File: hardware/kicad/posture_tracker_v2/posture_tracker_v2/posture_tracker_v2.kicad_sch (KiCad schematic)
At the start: 18 parts, among them J1 GCT_USB4135-GF-A, J2 JST-PH-2, U1 ESP32-S3-MINI-1U, U2 MPU-6050, U5 MCP73831T-2ACI/OT, U6 AP2112K-3.3TRG1

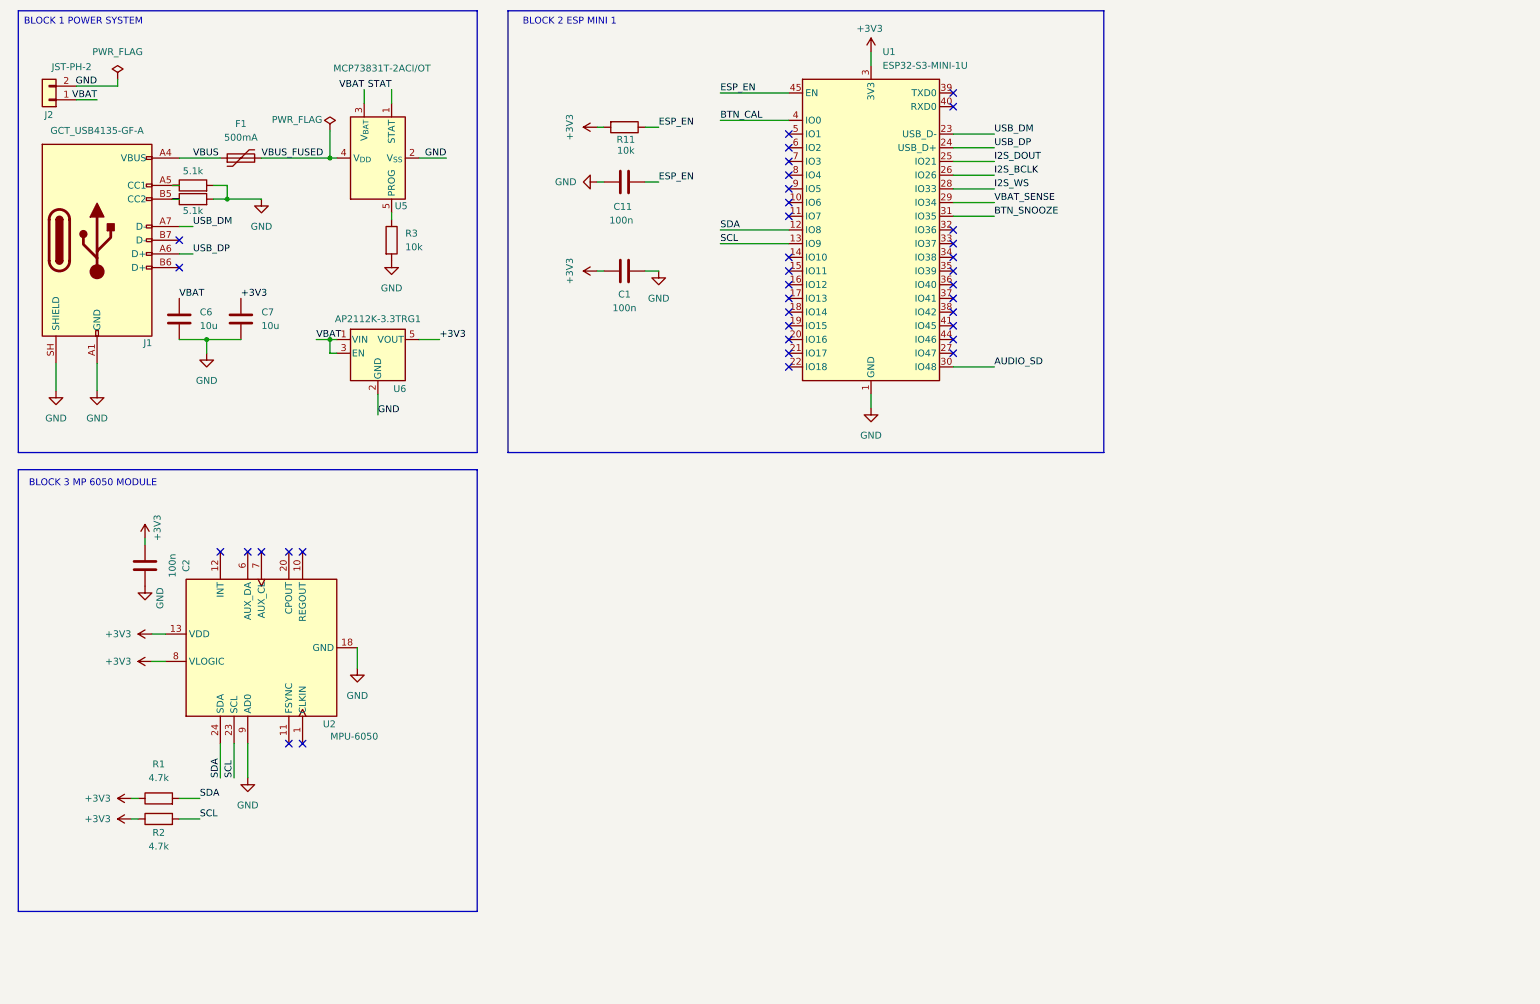
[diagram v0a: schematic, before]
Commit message: V2: apply Reddit review fixes — USB-C wiring, decoupling caps, footprint correction
- Fix USB-C B6/B7 cross-connection: A6+B7=D+, A7+B6=D- per USB-IF spec
  (diagonal pairing so both cable orientations work — previously B6/B7 had no net)
- Add C17 (4.7µF, 0402) on VBUS_FUSED for MCP73831 VDD decoupling
- Add C15 (10µF, 0805) bulk cap on ESP32-S3 VDD33 rail
- Add C16 (1µF, 0402) local bulk cap on DRV2605L VDD
- Fix U1 footprint: ESP32-S2-MINI-1 (52 pads) → ESP32-S3-MINI-1 (65 pads)
- Delete premature Gerbers (exported before routing — regenerate after routing)
- ERC clean: 0 errors, 5 warnings (all cosmetic/acceptable)
- DRC: 4 cosmetic silkscreen warnings, 148 unconnected pads (routing not done)
- Update all README docs: BOM (J1 connector, U7, new passives), schematics
  (all 7 blocks marked complete), PCB (layout in-progress), KICAD_CONTEXT
  (design decisions log, component table, session log), README_V2 (MCU/GPIO/connector)

Co-Authored-By: Claude Sonnet 4.6 <noreply@anthropic.com>
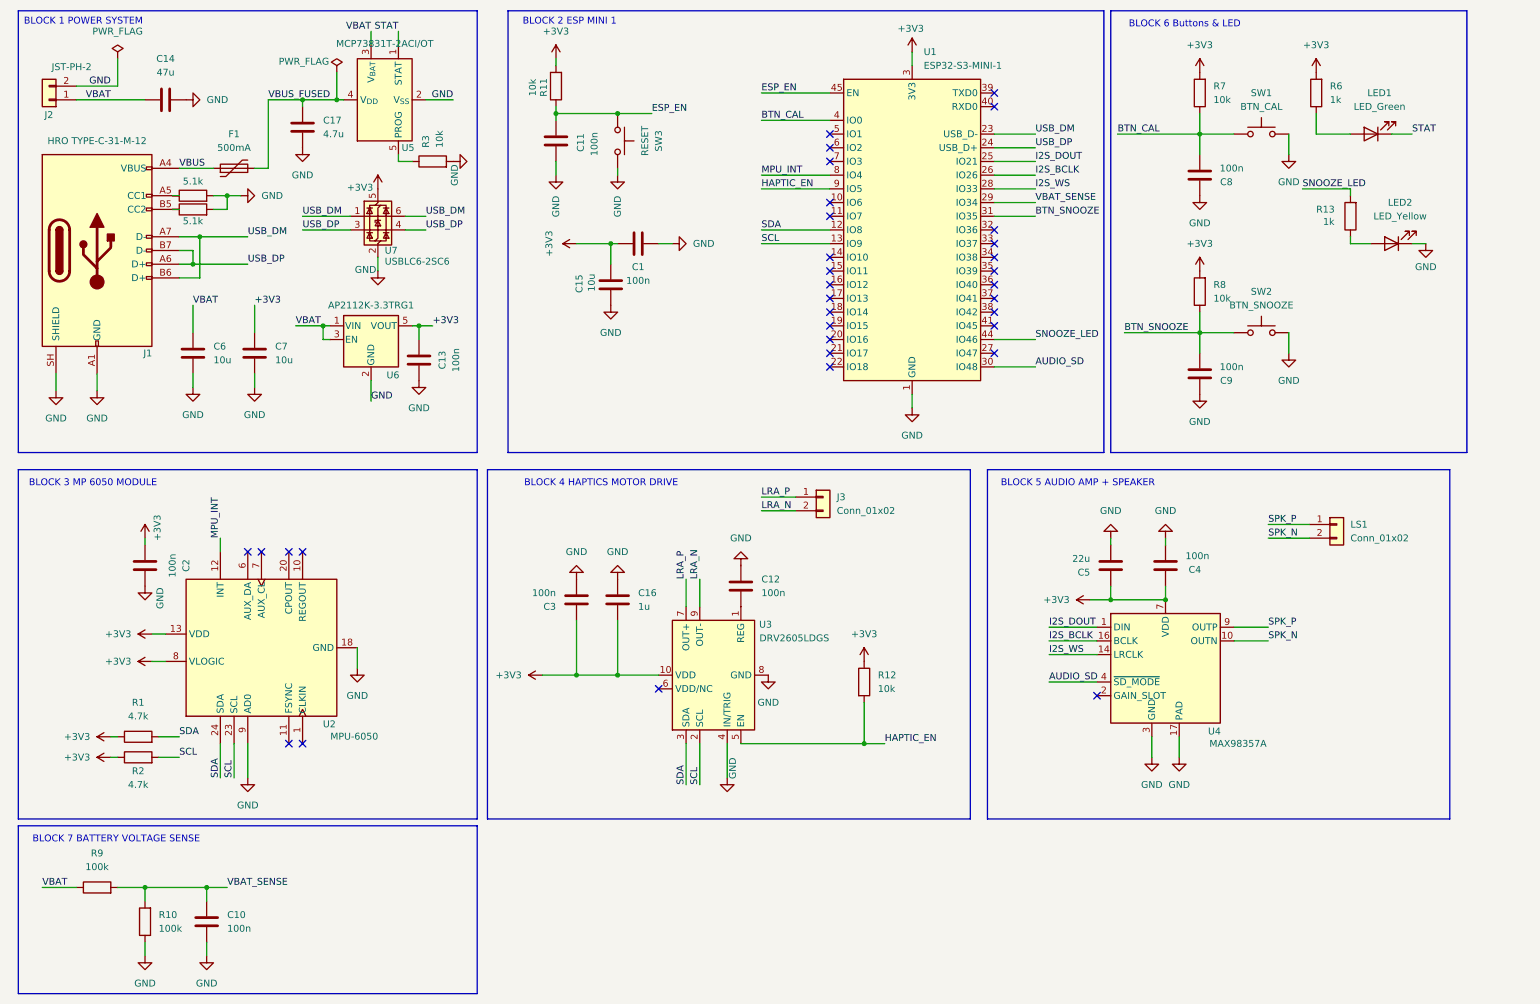
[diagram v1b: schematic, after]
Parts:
- added C10, C12, C13, C3, C4, C8, C9: 100n, Capacitor_SMD:C_0402_1005Metric, symbol Device:C
- added C14: 47u, Capacitor_SMD:C_0805_2012Metric, symbol Device:C
- added C15: 10u, Capacitor_SMD:C_0805_2012Metric, symbol Device:C
- added C16: 1u, Capacitor_SMD:C_0402_1005Metric, symbol Device:C
- added C17: 4.7u, Capacitor_SMD:C_01005_0402Metric, symbol Device:C
- added C5: 22u, Capacitor_SMD:C_0805_2012Metric, symbol Device:C
- added J3, LS1: Conn_01x02, Connector_PinHeader_2.54mm:PinHeader_1x02_P2.54mm_Vertical, symbol Connector_Generic:Conn_01x02
- added LED1: LED_Green, LED_SMD:LED_0805_2012Metric, symbol Device:LED
- added LED2: LED_Yellow, LED_SMD:LED_0805_2012Metric, symbol Device:LED
- added R10, R9: 100k, Resistor_SMD:R_0402_1005Metric, symbol Device:R
- added R12, R7, R8: 10k, Resistor_SMD:R_0402_1005Metric, symbol Device:R
- added R13, R6: 1k, Resistor_SMD:R_0402_1005Metric, symbol Device:R
- added SW1: BTN_CAL, SKRPABE010:SW_SKRPABE010, symbol Switch:SW_Push
- added SW2: BTN_SNOOZE, SKRPABE010:SW_SKRPABE010, symbol Switch:SW_Push
- added SW3: RESET, SKRPABE010:SW_SKRPABE010, symbol Switch:SW_Push
- added U3: DRV2605LDGS, Package_SO:TSSOP-10_3x3mm_P0.5mm, symbol Driver:DRV2605LDGS
- added U4: MAX98357A, Package_DFN_QFN:TQFN-16-1EP_3x3mm_P0.5mm_EP1.23x1.23mm, symbol Audio:MAX98357A
- added U7: USBLC6-2SC6, Package_TO_SOT_SMD:SOT-23-6, symbol Power_Protection:USBLC6-2SC6
- C1, C11, C2: footprint (none) -> Capacitor_SMD:C_0402_1005Metric
- C6, C7: footprint (none) -> Capacitor_SMD:C_0805_2012Metric
- F1: footprint (none) -> Fuse:Fuse_0805_2012Metric
- J1: value GCT_USB4135-GF-A -> HRO TYPE-C-31-M-12; footprint (none) -> Connector_USB:USB_C_Receptacle_HRO_TYPE-C-31-M-12
- J2: footprint (none) -> Connector_JST:JST_PH_S2B-PH-K_1x02_P2.00mm_Horizontal
- R1, R11, R2, R3, R4, R5: footprint (none) -> Resistor_SMD:R_0402_1005Metric
- U1: value ESP32-S3-MINI-1U -> ESP32-S3-MINI-1; footprint PCM_Espressif:ESP32-S3-MINI-1U -> RF_Module:ESP32-S2-MINI-1
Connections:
- net +3V3: now also C13.2, C15.2, C16.2, C3.1, C4.1, C5.1, R12.1, R6.2, R7.2, R8.2, U3.10 (VDD), U4.7 (VDD), U4.8 (VDD), U7.5 (VBUS)
- net AUDIO_SD: now also U4.4 (~{SD_MODE})
- net BTN_CAL: now also C8.2, R7.1, SW1.1
- net BTN_SNOOZE: now also C9.2, R8.1, SW2.1
- net ESP_EN: now also SW3.1
- net GND: now also C10.2, C12.2, C13.1, C14.2, C15.1, C16.1, C17.1, C3.2, C4.2, C5.2, C8.1, C9.1, LED2.1 (K), R10.1, SW1.2, SW2.2, SW3.2, U3.4 (IN/TRIG), U3.8 (GND), U4.11 (GND), U4.15 (GND), U4.17 (PAD), U4.3 (GND), U7.2 (GND)
- net I2S_BCLK: now also U4.16 (BCLK)
- net I2S_DOUT: now also U4.1 (DIN)
- net I2S_WS: now also U4.14 (LRCLK)
- net SCL: now also U3.2 (SCL)
- net SDA: now also U3.3 (SDA)
- net STAT: now also LED1.1 (K)
- net USB_DM: now also J1.B6 (D+), U7.1 (I/O1), U7.6 (I/O1)
- net USB_DP: now also J1.B7 (D-), U7.3 (I/O2), U7.4 (I/O2)
- net VBAT: now also C14.1, R9.1
- net VBAT_SENSE: now also C10.1, R10.2, R9.2
- net VBUS_FUSED: now also C17.2
- net SNOOZE_LED: now reaches U1.44 (IO46)
- net SNOOZE_LED: now also R13.2
- net MPU_INT: now reaches U1.8 (IO4)
- net MPU_INT: now also U2.12 (INT)
- net HAPTIC_EN: now reaches U1.9 (IO5)
- net HAPTIC_EN: now also R12.2, U3.5 (EN)
- new net: LED1.2 (A), R6.1
- new net: C12.1, U3.1 (REG)
- new net: LED2.2 (A), R13.1
- new net LRA_N: J3.2 (Pin_2), U3.9 (OUT-)
- new net LRA_P: J3.1 (Pin_1), U3.7 (OUT+)
- new net SPK_N: LS1.2 (Pin_2), U4.10 (OUTN)
- new net SPK_P: LS1.1 (Pin_1), U4.9 (OUTP)
- no-connect marks 37 -> 33
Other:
- note added: "BLOCK 4 HAPTICS MOTOR DRIVE"
- note added: "BLOCK 5 AUDIO AMP + SPEAKER"
- note added: "BLOCK 6 Buttons & LED"
- note added: "BLOCK 7 BATTERY VOLTAGE SENSE"
- company: (none) -> Made By Kiran
- title: (none) -> Posture Tracker
- moved on the sheet: C1, C11, C6, C7, F1, J1, R1, R11, R2, R3, U1, U5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

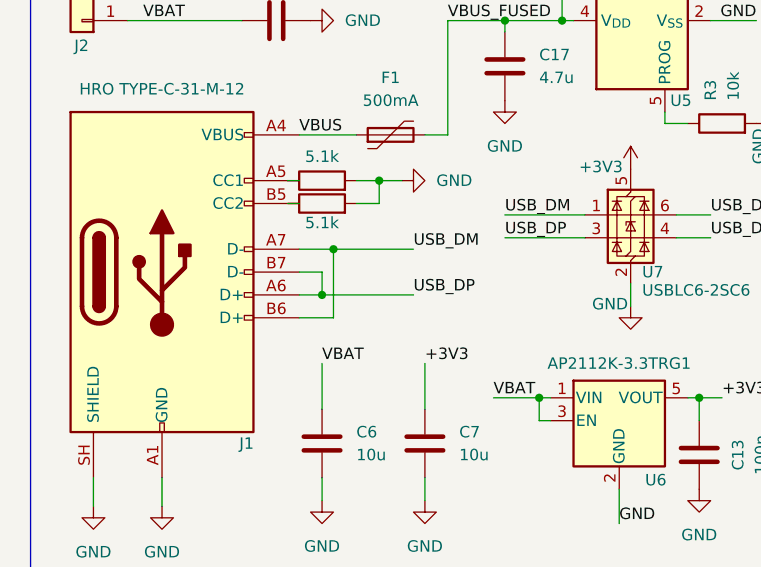
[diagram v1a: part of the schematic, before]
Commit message: WIP: PCB layout routing setup — clean DRC baseline, connector updates
- PCB: cleared all routing, established clean DRC baseline (154 unconnected,
  2 acceptable silk warnings for U1 antenna overhang, 0 copper errors)
- PCB: GND routing strategy decided — B.Cu copper pour filled at end,
  no manual GND traces; Power/Default net classes configured
- Schematic: J3 (LRA) and LS1 (speaker) connector footprints set to
  JST GH 1.25mm vertical to match physical cable connectors on
  Vybronics LRA and MECCANIXITY 20mm speaker
- .gitignore: added DS_Store, KiCad lock/backup/temp files, KiCad plot PDFs
- README_V2.md: updated Phase 10 status, added PCB layout state section
- hardware/pcb/README.md: updated routing progress tracker
- hardware/schematics/README.md: added connector decision table

Routing order: +3V3 → VBAT → VBUS → I2C → I2S → USB → signals → GND pour

Co-Authored-By: Claude Sonnet 4.6 <noreply@anthropic.com>
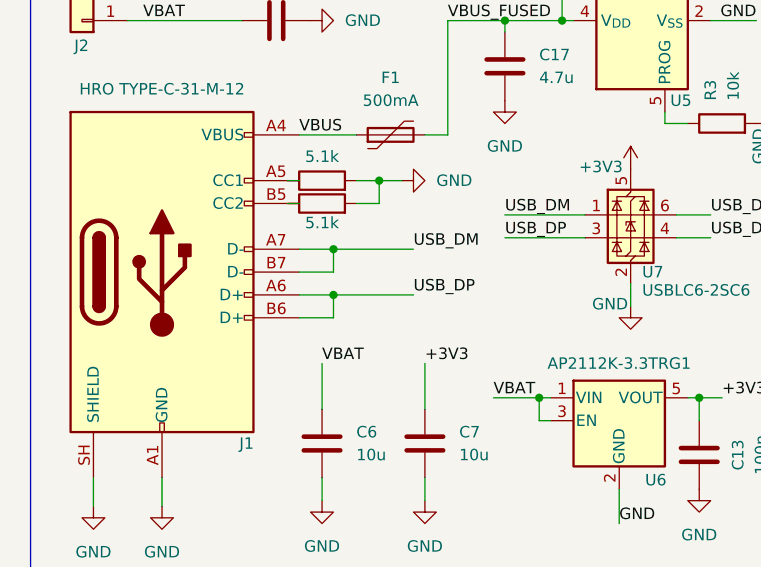
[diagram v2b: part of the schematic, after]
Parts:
- C17: footprint Capacitor_SMD:C_01005_0402Metric -> Capacitor_SMD:C_0402_1005Metric
- LS1: footprint Connector_PinHeader_2.54mm:PinHeader_1x02_P2.54mm_Vertical -> Connector_JST:JST_GH_BM02B-GHS-TBT_1x02-1MP_P1.25mm_Vertical
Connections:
- net USB_DM: now also J1.B7 (D-); no longer J1.B6 (D+)
- net USB_DP: now also J1.B6 (D+); no longer J1.B7 (D-)
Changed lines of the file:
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@@
 	)
 	(junction
+		(at 48.26 60.96)
+		(diameter 0)
+		(color 0 0 0 0)
+	)
+	(junction
 		(at 217.17 123.19)
 		(diameter 0)
@@
 	)
 	(junction
-		(at 46.99 60.96)
-		(diameter 0)
-		(color 0 0 0 0)
-	)
-	(junction
 		(at 171.45 149.86)
 		(diameter 0)
@@
 	(wire
 		(pts
-			(xy 44.45 58.42) (xy 46.99 58.42)
+			(xy 44.45 58.42) (xy 48.26 58.42)
+		)
+		(stroke
+			(width 0)
+			(type default)
+		)
+	)
+	(wire
+		(pts
+			(xy 48.26 60.96) (xy 57.15 60.96)
 		)
 		(stroke
@@
 	(wire
 		(pts
+			(xy 48.26 55.88) (xy 57.15 55.88)
+		)
+		(stroke
+			(width 0)
+			(type default)
+		)
+	)
+	(wire
+		(pts
 			(xy 205.74 133.35) (xy 214.63 133.35)
 		)
@@
 	(wire
 		(pts
-			(xy 46.99 58.42) (xy 46.99 60.96)
-		)
-		(stroke
-			(width 0)
-			(type default)
-		)
-	)
-	(wire
-		(pts
 			(xy 71.12 72.39) (xy 72.39 72.39)
 		)
@@
 	(wire
 		(pts
-			(xy 48.26 55.88) (xy 57.15 55.88)
-		)
-		(stroke
-			(width 0)
-			(type default)
-		)
-	)
-	(wire
-		(pts
 			(xy 44.45 55.88) (xy 48.26 55.88)
 		)
@@
 	(wire
 		(pts
-			(xy 44.45 60.96) (xy 46.99 60.96)
+			(xy 44.45 60.96) (xy 48.26 60.96)
 		)
 		(stroke
@@
 	(wire
 		(pts
-			(xy 46.99 60.96) (xy 57.15 60.96)
+			(xy 140.97 119.38) (xy 140.97 124.46)
 		)
 		(stroke
@@
 	(wire
 		(pts
-			(xy 140.97 119.38) (xy 140.97 124.46)
+			(xy 48.26 55.88) (xy 48.26 58.42)
 		)
 		(stroke
@@
 	(wire
 		(pts
-			(xy 118.11 57.15) (xy 124.46 57.15)
+			(xy 48.26 60.96) (xy 48.26 63.5)
 		)
 		(stroke
@@
 	(wire
 		(pts
-			(xy 88.9 72.39) (xy 91.44 72.39)
+			(xy 118.11 57.15) (xy 124.46 57.15)
 		)
 		(stroke
@@
 	(wire
 		(pts
-			(xy 48.26 63.5) (xy 48.26 55.88)
+			(xy 88.9 72.39) (xy 91.44 72.39)
 		)
 		(stroke
@@
 			)
 		)
-		(property "Footprint" "Capacitor_SMD:C_01005_0402Metric"
+		(property "Footprint" "Capacitor_SMD:C_0402_1005Metric"
 			(at 66.3448 31.75 0)
 			(hide yes)
@@
 			)
 		)
-		(property "Footprint" "Connector_PinHeader_2.54mm:PinHeader_1x02_P2.54mm_Vertical"
+		(property "Footprint" "Connector_JST:JST_GH_BM02B-GHS-TBT_1x02-1MP_P1.25mm_Vertical"
 			(at 259.08 109.22 0)
 			(hide yes)

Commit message: V2: update KiCad schematic — Block 4 routing and component updates
Co-Authored-By: Claude Sonnet 4.6 <noreply@anthropic.com>
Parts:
- added C18, C19: 220p, Capacitor_SMD:C_0805_2012Metric, symbol Device:C
- added FB1: FerriteBead_Small, Inductor_SMD:L_01005_0402Metric, symbol Device:FerriteBead_Small
- added FB2: FerriteBead_Small, symbol Device:FerriteBead_Small
- added R14: 1M, Resistor_SMD:R_0402_1005Metric, symbol Device:R
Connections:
- net +3V3: now also R14.1
- net AUDIO_SD: now also R14.2
- net GND: now also C18.1, C19.1
- net SPK_N: now also C19.2, FB2.2; no longer U4.10 (OUTN)
- net SPK_P: now also C18.2, FB1.2; no longer U4.9 (OUTP)
- new net: FB2.1, U4.10 (OUTN)
- new net: FB1.1, U4.9 (OUTP)

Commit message: V2: update speaker and motor connectors to Molex PicoBlade 53047-0210
LS1 (speaker): JST GH 1.25mm → Molex PicoBlade 53047-0210
  GH was wrong — wire too thick to crimp, fiddly for hand assembly.
  PicoBlade is 1.25mm pitch, low-profile, looks clean in 3D render,
  correct gauge for thin speaker wire leads.

J3 → M1 (LRA motor): 2.54mm pin header → Molex PicoBlade 53047-0210
  Renamed J3 to M1 to match BOM/CLAUDE.md reference. Same connector
  as LS1 for consistency — motor wire leads same gauge as speaker.

Both use: Connector_Molex:Molex_PicoBlade_53047-0210_1x02-1MP_P1.25mm_Vertical

Co-Authored-By: Claude Sonnet 4.6 <noreply@anthropic.com>
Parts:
- LS1: value Conn_01x02 -> Molex_PicoBlade_53047-0210; footprint Connector_JST:JST_GH_BM02B-GHS-TBT_1x02-1MP_P1.25mm_Vertical -> Connector_Molex:Molex_PicoBlade_53047-0210_1x02-1MP_P1.25mm_Vertical
- M1: renamed from J3; value Conn_01x02 -> Molex_PicoBlade_53047-0210; footprint Connector_PinHeader_2.54mm:PinHeader_1x02_P2.54mm_Vertical -> Connector_Molex:Molex_PicoBlade_53047-0210_1x02-1MP_P1.25mm_Vertical
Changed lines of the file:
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@@
 			)
 		)
-		(property "Value" "Conn_01x02"
+		(property "Value" "Molex_PicoBlade_53047-0210"
 			(at 261.62 111.7599 0)
 			(show_name no)
@@
 			)
 		)
-		(property "Footprint" "Connector_JST:JST_GH_BM02B-GHS-TBT_1x02-1MP_P1.25mm_Vertical"
+		(property "Footprint" "Connector_Molex:Molex_PicoBlade_53047-0210_1x02-1MP_P1.25mm_Vertical"
 			(at 259.08 109.22 0)
 			(hide yes)
@@
 		(dnp no)
 		(fields_autoplaced yes)
-		(property "Reference" "J3"
+		(property "Reference" "M1"
 			(at 166.37 104.1399 0)
 			(show_name no)
@@
 			)
 		)
-		(property "Value" "Conn_01x02"
+		(property "Value" "Molex_PicoBlade_53047-0210"
 			(at 166.37 106.6799 0)
 			(show_name no)
@@
 			)
 		)
-		(property "Footprint" "Connector_PinHeader_2.54mm:PinHeader_1x02_P2.54mm_Vertical"
+		(property "Footprint" "Connector_Molex:Molex_PicoBlade_53047-0210_1x02-1MP_P1.25mm_Vertical"
 			(at 163.83 104.14 0)
 			(hide yes)
@@
 			(project "posture_tracker_v2"
 				(path "/ed2b0582-7f4b-4ec5-a143-e23922c2754c"
-					(reference "J3")
+					(reference "M1")
 					(unit 1)
 				)

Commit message: V2: update PCB footprints and 3D models for LS1 and M1
LS1 and M1 footprints updated in PCB from old connectors to
Molex PicoBlade 53047-0210 (1x02, 1.25mm vertical).
3D model assigned: Molex_PicoBlade_53398-0271_1x02-1MP_P1.25mm_Vertical.step
Schematic 4-char value fix included.

Co-Authored-By: Claude Sonnet 4.6 <noreply@anthropic.com>
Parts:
- LS1, M1: footprint Connector_Molex:Molex_PicoBlade_53047-0210_1x02-1MP_P1.25mm_Vertical -> Connector_Molex:Molex_PicoBlade_53047-0210_1x02_P1.25mm_Vertical
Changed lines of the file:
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@@
 			)
 		)
-		(property "Footprint" "Connector_Molex:Molex_PicoBlade_53047-0210_1x02-1MP_P1.25mm_Vertical"
+		(property "Footprint" "Connector_Molex:Molex_PicoBlade_53047-0210_1x02_P1.25mm_Vertical"
 			(at 259.08 109.22 0)
 			(hide yes)
@@
 			)
 		)
-		(property "Footprint" "Connector_Molex:Molex_PicoBlade_53047-0210_1x02-1MP_P1.25mm_Vertical"
+		(property "Footprint" "Connector_Molex:Molex_PicoBlade_53047-0210_1x02_P1.25mm_Vertical"
 			(at 163.83 104.14 0)
 			(hide yes)
